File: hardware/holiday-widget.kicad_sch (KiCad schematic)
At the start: 5 parts, among them J2 UART, J33 Conn_ARM_JTAG_SWD_10, J4 BATTERY POWER, J5 VDC POWER

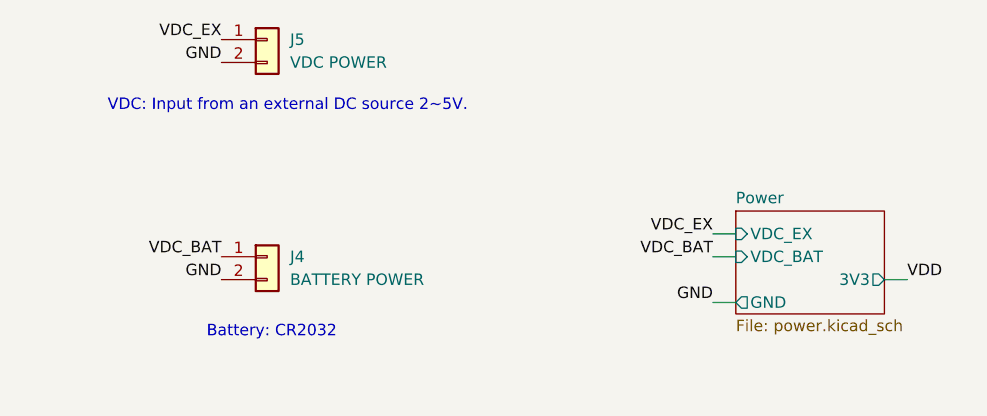
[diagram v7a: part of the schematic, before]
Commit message: Remove external power connector
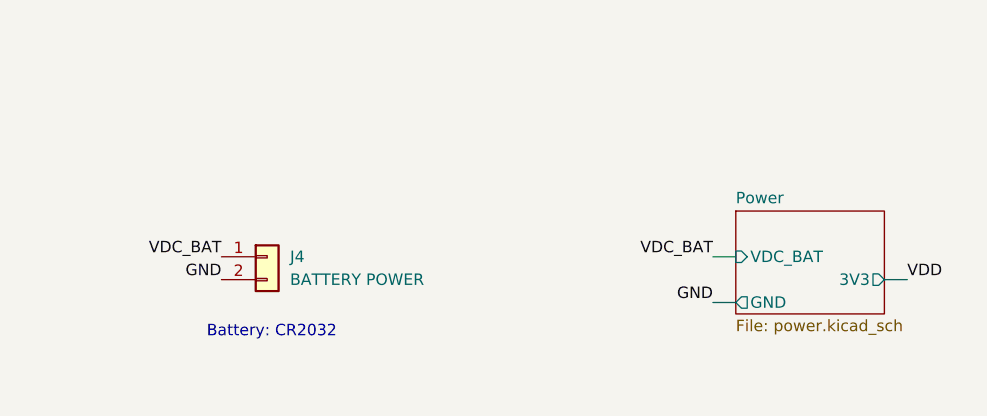
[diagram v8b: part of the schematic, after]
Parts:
- removed J5: VDC POWER, Connector_Wire:SolderWire-1sqmm_1x02_P5.4mm_D1.4mm_OD2.7mm, symbol Connector_Generic:Conn_01x02
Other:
- sheet Power ports: added none; removed VDC_EX
- note removed: "VDC: Input from an external DC source 2~5V."
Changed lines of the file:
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@@
-	(wire
-		(pts
-			(xy 111.76 50.8) (xy 114.3 50.8)
-		)
-		(stroke
-			(width 0)
-			(type default)
-		)
-	)
 	(wire
 		(pts
@@
 			(width 0)
 			(type default)
-		)
-	)
-	(text "VDC: Input from an external DC source 2~5V."
-		(exclude_from_sim no)
-		(at 64.516 36.576 0)
-		(effects
-			(font
-				(size 1.27 1.27)
-			)
 		)
 	)
@@
 		)
 	)
-	(label "VDC_EX"
-		(at 57.15 29.21 180)
-		(fields_autoplaced yes)
-		(effects
-			(font
-				(size 1.27 1.27)
-			)
-			(justify right bottom)
-		)
-	)
 	(label "GND"
 		(at 106.68 92.71 180)
@@
 	(label "VDD"
 		(at 247.65 97.79 180)
-		(fields_autoplaced yes)
-		(effects
-			(font
-				(size 1.27 1.27)
-			)
-			(justify right bottom)
-		)
-	)
-	(label "GND"
-		(at 57.15 31.75 180)
-		(fields_autoplaced yes)
-		(effects
-			(font
-				(size 1.27 1.27)
-			)
-			(justify right bottom)
-		)
-	)
-	(label "VDC_EX"
-		(at 111.76 50.8 180)
 		(fields_autoplaced yes)
 		(effects
@@
 	)
 	(symbol
-		(lib_id "Connector_Generic:Conn_01x02")
-		(at 62.23 29.21 0)
-		(unit 1)
-		(exclude_from_sim no)
-		(in_bom yes)
-		(on_board yes)
-		(dnp no)
-		(fields_autoplaced yes)
-		(property "Reference" "J5"
-			(at 64.77 29.2099 0)
-			(effects
-				(font
-					(size 1.27 1.27)
-				)
-				(justify left)
-			)
-		)
-		(property "Value" "VDC POWER"
-			(at 64.77 31.7499 0)
-			(effects
-				(font
-					(size 1.27 1.27)
-				)
-				(justify left)
-			)
-		)
-		(property "Footprint" "Connector_Wire:SolderWire-1sqmm_1x02_P5.4mm_D1.4mm_OD2.7mm"
-			(at 62.23 29.21 0)
-			(effects
-				(font
-					(size 1.27 1.27)
-				)
-				(hide yes)
-			)
-		)
-		(property "Datasheet" "~"
-			(at 62.23 29.21 0)
-			(effects
-				(font
-					(size 1.27 1.27)
-				)
-				(hide yes)
-			)
-		)
-		(property "Description" "Generic connector, single row, 01x02, script generated (kicad-library-utils/schlib/autogen/connector/)"
-			(at 62.23 29.21 0)
-			(effects
-				(font
-					(size 1.27 1.27)
-				)
-				(hide yes)
-			)
-		)
-		(property "MPN" ""
-			(at 62.23 29.21 0)
-			(effects
-				(font
-					(size 1.27 1.27)
-				)
-				(hide yes)
-			)
-		)
-		(pin "2"
-		)
-		(pin "1"
-		)
-		(instances
-			(project "holiday-widget"
-				(path "/addc3208-a9c4-4d28-9808-559c1d81e43b"
-					(reference "J5")
-					(unit 1)
-				)
-			)
-		)
-	)
-	(symbol
 		(lib_id "power:PWR_FLAG")
 		(at 191.77 67.31 0)
@@
 			)
 		)
-		(pin "VDC_EX" input
-			(at 114.3 50.8 180)
-			(effects
-				(font
-					(size 1.27 1.27)
-				)
-				(justify left)
-			)
-		)
